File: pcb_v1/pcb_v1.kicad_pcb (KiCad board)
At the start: 2 copper layers, 57.5 x 32 mm, 14 parts, among them IC1 ESP32-C3-WROOM-02-N4, IC2 DWM3000TR13, IC3 TC1017-3.3VLTTR, J1 Conn_01x04_Pin, J2 1769, J3 Conn_01x04_Pin

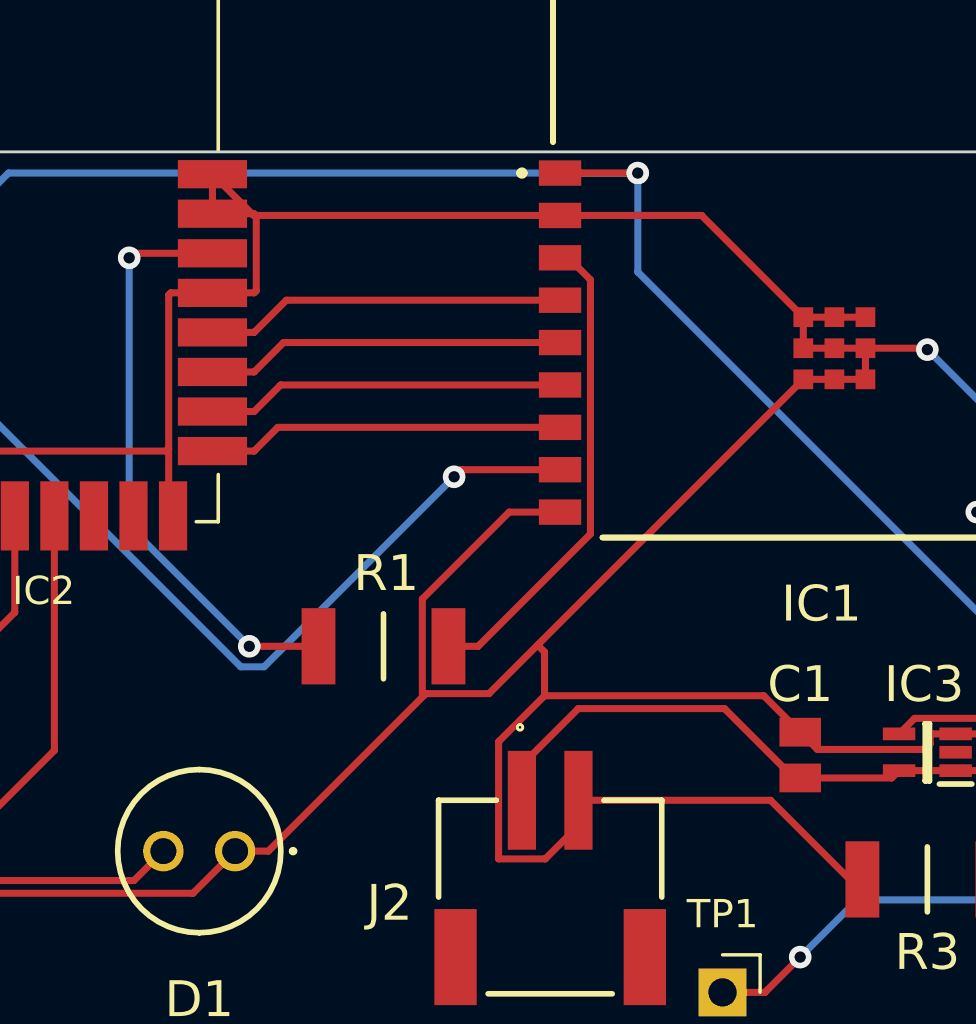
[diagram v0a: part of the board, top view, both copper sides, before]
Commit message: fix wiring issue, EN pin on esp32 always grounded
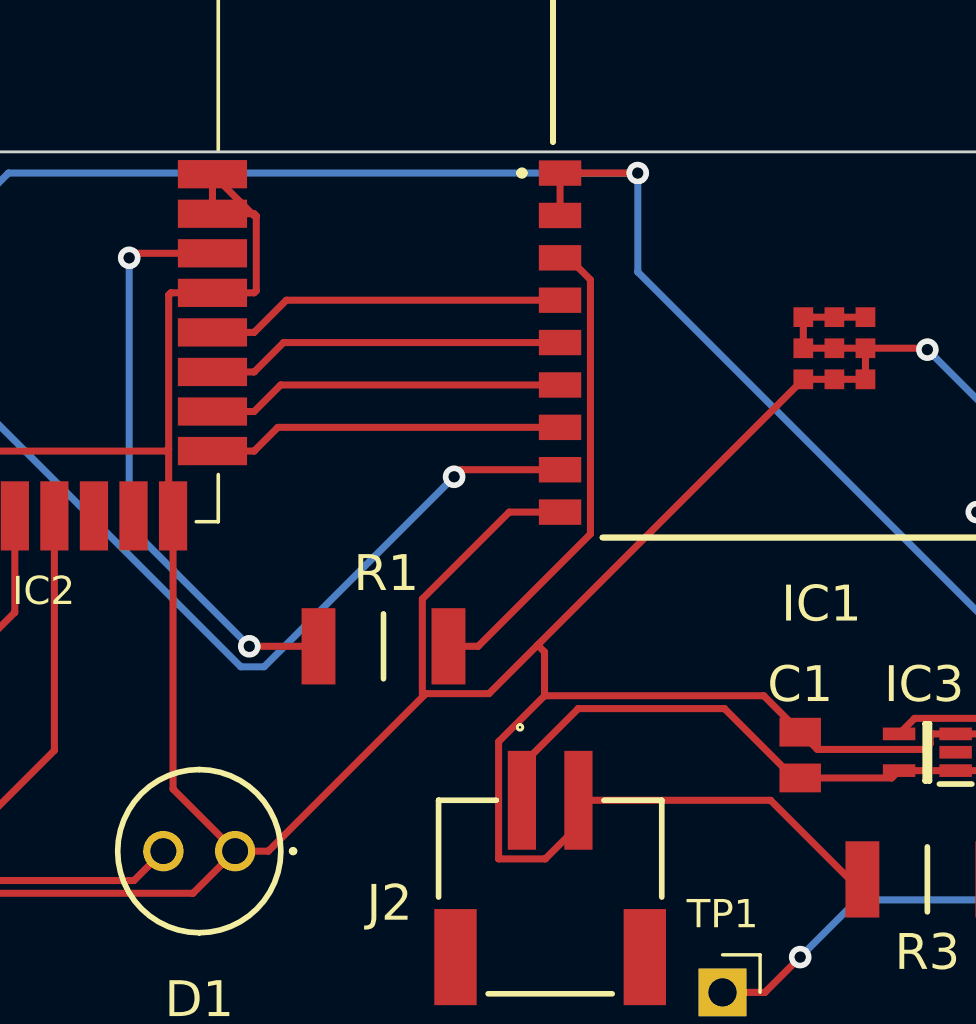
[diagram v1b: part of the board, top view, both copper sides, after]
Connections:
- IC1 pad 2: GND -> VDD
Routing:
- net GND: track 199.6 -> 191.4 mm
- net VDD: track 102.5 -> 104.0 mm
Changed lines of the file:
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@@
     (pad_to_mask_clearance 0)
     (pcbplotparams
-      (layerselection 0x7ffffff_ffffffff)
+      (layerselection 0x00050fc_ffffffff)
       (plot_on_all_layers_selection 0x0000000_00000000)
       (disableapertmacros false)
-      (usegerberextensions false)
+      (usegerberextensions true)
       (usegerberattributes true)
       (usegerberadvancedattributes true)
-      (creategerberjobfile true)
+      (creategerberjobfile false)
       (dashed_line_dash_ratio 12.000000)
       (dashed_line_gap_ratio 3.000000)
@@
       (plotinvisibletext false)
       (sketchpadsonfab false)
-      (subtractmaskfromsilk false)
+      (subtractmaskfromsilk true)
       (outputformat 1)
       (mirror false)
@@
       (net 3 "VDD") (pinfunction "3V3") (pintype "passive"))
     (pad "2" smd rect (at -9.71 -4.7 90) (size 0.9 1.5) (layers "F.Cu" "F.Paste" "F.Mask")
-      (net 2 "GND") (pinfunction "EN") (pintype "passive"))
+      (net 3 "VDD") (pinfunction "EN") (pintype "passive"))
     (pad "3" smd rect (at -9.71 -3.2 90) (size 0.9 1.5) (layers "F.Cu" "F.Paste" "F.Mask")
       (net 4 "Net-(IC1-IO4)") (pinfunction "IO4") (pintype "passive"))
@@
   (segment (start 110.8025 97.885) (end 110.6475 97.73) (width 0.25) (layer "F.Cu") (net 2))
   (segment (start 137.6 105.675) (end 137.6 105.95) (width 0.25) (layer "F.Cu") (net 2))
-  (segment (start 129.51 87.25) (end 133.11 90.85) (width 0.25) (layer "F.Cu") (net 2))
   (segment (start 119.75 104.175) (end 121.985 104.175) (width 0.25) (layer "F.Cu") (net 2))
   (segment (start 112.1975 85.79) (end 113.6575 87.25) (width 0.25) (layer "F.Cu") (net 2))
@@
   (segment (start 119.625 100.825) (end 119.625 104.175) (width 0.25) (layer "F.Cu") (net 2))
   (segment (start 122.325 105.875) (end 122.325 110.025) (width 0.25) (layer "F.Cu") (net 2))
+  (segment (start 113 109.75) (end 110.8025 107.5525) (width 0.25) (layer "F.Cu") (net 2))
   (segment (start 148.505 112.755) (end 145.5 109.75) (width 0.25) (layer "F.Cu") (net 2))
   (segment (start 119.625 104.175) (end 119.75 104.175) (width 0.25) (layer "F.Cu") (net 2))
@@
   (segment (start 138.5 105.6) (end 137.675 105.6) (width 0.25) (layer "F.Cu") (net 2))
   (segment (start 123.95 104.25) (end 123.95 102.7) (width 0.25) (layer "F.Cu") (net 2))
-  (segment (start 124.5 87.25) (end 129.51 87.25) (width 0.25) (layer "F.Cu") (net 2))
   (segment (start 135.2 110.75) (end 134.75 110.75) (width 0.25) (layer "F.Cu") (net 2))
   (segment (start 135.31 93.05) (end 134.21 93.05) (width 0.25) (layer "F.Cu") (net 2))
@@
   (segment (start 113.6725 87.19) (end 113.7475 87.265) (width 0.25) (layer "F.Cu") (net 2))
   (segment (start 142.025 107.16) (end 140.465 105.6) (width 0.25) (layer "F.Cu") (net 2))
+  (segment (start 110.8025 107.5525) (end 110.8025 97.885) (width 0.25) (layer "F.Cu") (net 2))
   (segment (start 110.7225 89.99) (end 112.1975 89.99) (width 0.25) (layer "F.Cu") (net 2))
   (segment (start 133.11 91.95) (end 134.21 91.95) (width 0.25) (layer "F.Cu") (net 2))
@@
   (segment (start 110.5575 95.59) (end 110.6475 95.5) (width 0.25) (layer "F.Cu") (net 2))
   (segment (start 123.975 110.025) (end 125.15 108.85) (width 0.25) (layer "F.Cu") (net 2))
-  (segment (start 113.6575 87.25) (end 124.5 87.25) (width 0.25) (layer "F.Cu") (net 2))
   (segment (start 137.45 91.95) (end 137.5 92) (width 0.25) (layer "F.Cu") (net 2))
   (segment (start 133.11 90.85) (end 134.21 90.85) (width 0.25) (layer "F.Cu") (net 2))
@@
   (segment (start 145.5 100) (end 137.5 92) (width 0.25) (layer "B.Cu") (net 2))
   (segment (start 124.5 85.75) (end 127.25 85.75) (width 0.25) (layer "F.Cu") (net 3))
+  (segment (start 124.5 87.25) (end 124.5 85.75) (width 0.25) (layer "F.Cu") (net 3))
   (segment (start 142.25 104.25) (end 142 104) (width 0.25) (layer "F.Cu") (net 3))
   (segment (start 101.93 103.25) (end 102 103.32) (width 0.25) (layer "F.Cu") (net 3))
